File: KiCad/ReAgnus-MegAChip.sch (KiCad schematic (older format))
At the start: 40 parts, among them J3 Conn_01x03, J4 Conn_01x01, J5 Conn_01x01, J6 Conn_01x01, J7 Conn_01x01, U1 PLCC-84-Plug, U2 LM1117-3.3, U3 SN74CBTD16210, U4 SN74CBTD16210, U5 SN74CBTD16210, U6 SN74CBTD16210, U8 74LVC1G07, U9 Agnus_TH_plug_pins

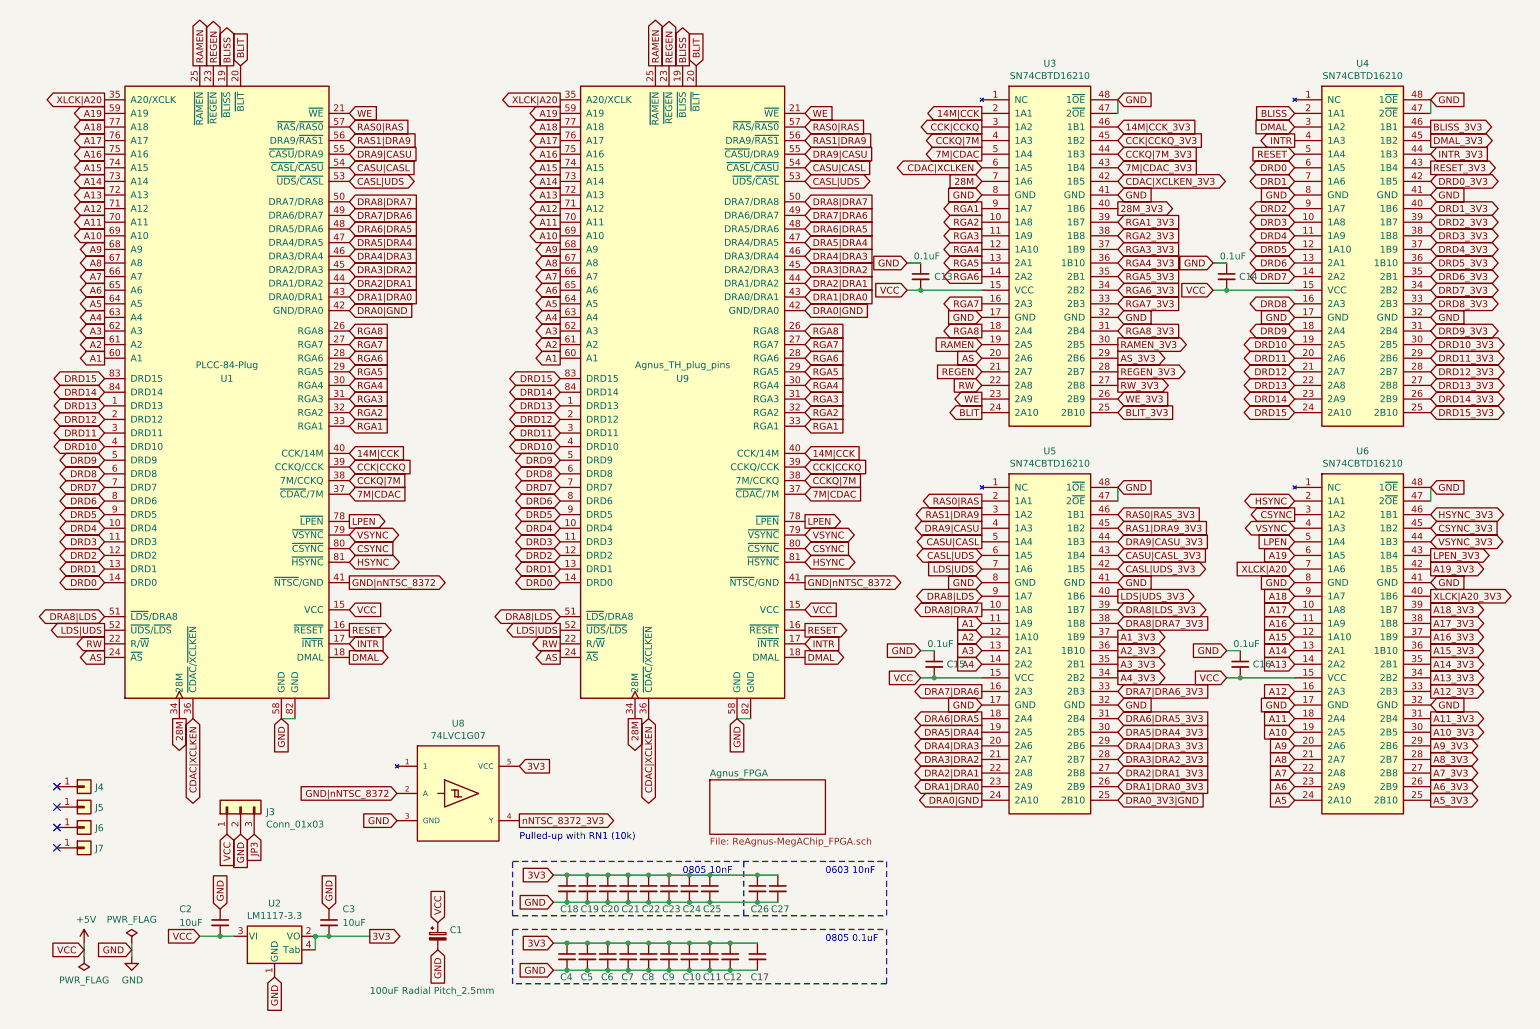
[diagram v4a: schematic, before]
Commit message: fixed typo XLCK to XCLK on (XCLK/A20) net
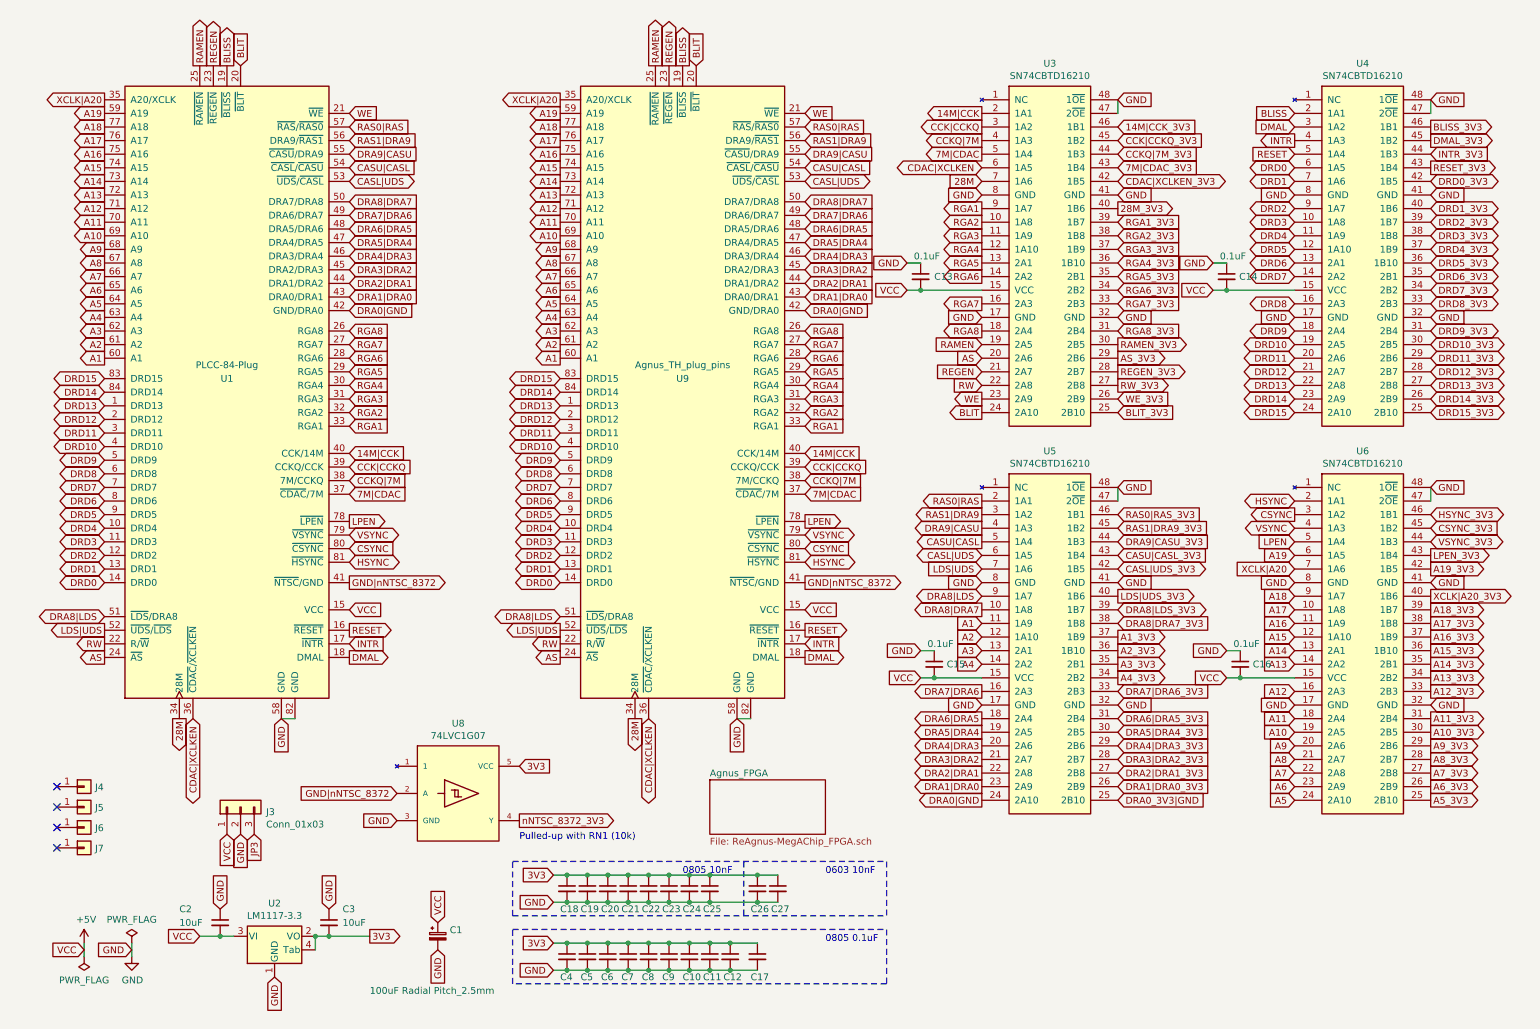
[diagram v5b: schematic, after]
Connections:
- net XLCK|A20 renamed XCLK|A20
- net XLCK|A20_3V3 renamed XCLK|A20_3V3
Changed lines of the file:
@@
 DRD0
 Text GLabel 1000 1150 0    50   Output ~ 0
-XLCK|A20
+XCLK|A20
 Text GLabel 1000 3050 0    50   Output ~ 0
 A1
@@
 DRD15
 Text GLabel 9750 4600 0    50   Input ~ 0
-XLCK|A20
+XCLK|A20
 Text GLabel 7450 4800 0    50   BiDi ~ 0
 DRA8|LDS
@@
 DRD0
 Text GLabel 4350 1150 0    50   Output ~ 0
-XLCK|A20
+XCLK|A20
 Text GLabel 4350 3050 0    50   Output ~ 0
 A1
@@
 GND
 Text GLabel 10750 4800 2    50   Output ~ 0
-XLCK|A20_3V3
+XCLK|A20_3V3
 Text GLabel 10750 4000 2    50   Input ~ 0
 GND

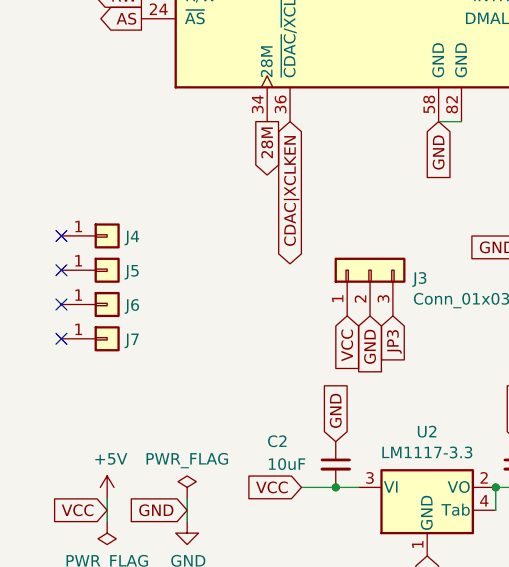
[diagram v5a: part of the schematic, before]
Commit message: Changed to 6 mil routing and to updated PLCC-footprint with 0.6mm pinholes and fixed dimensions for homebrew PLCC-84-plug
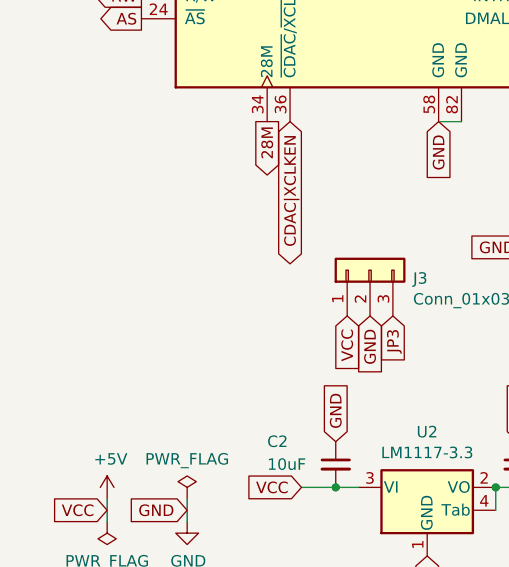
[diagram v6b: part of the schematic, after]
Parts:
- removed J4, J5, J6, J7: Conn_01x01, Connector_PinHeader_2.54mm:PinHeader_1x01_P2.54mm_Vertical, symbol Connector_Generic:Conn_01x01
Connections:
- no-connect marks 4 -> 0
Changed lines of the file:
@@
 Text GLabel 1000 5250 0    50   Output ~ 0
 AS
-$Comp
-L Connector_Generic:Conn_01x01 J4
-U 1 1 60D1FBEB
-P 850 6200
-F 0 "J4" H 930 6196 50  0000 L CNN
-F 1 "Conn_01x01" H 930 6151 50  0001 L CNN
-F 2 "Connector_PinHeader_2.54mm:PinHeader_1x01_P2.54mm_Vertical" H 850 6200 50  0001 C CNN
-F 3 "~" H 850 6200 50  0001 C CNN
-	1    850  6200
-	1    0    0    -1
-$EndComp
-$Comp
-L Connector_Generic:Conn_01x01 J5
-U 1 1 60D20CDD
-P 850 6350
-F 0 "J5" H 930 6346 50  0000 L CNN
-F 1 "Conn_01x01" H 930 6301 50  0001 L CNN
-F 2 "Connector_PinHeader_2.54mm:PinHeader_1x01_P2.54mm_Vertical" H 850 6350 50  0001 C CNN
-F 3 "~" H 850 6350 50  0001 C CNN
-	1    850  6350
-	1    0    0    -1
-$EndComp
-$Comp
-L Connector_Generic:Conn_01x01 J6
-U 1 1 60D21648
-P 850 6500
-F 0 "J6" H 930 6496 50  0000 L CNN
-F 1 "Conn_01x01" H 930 6451 50  0001 L CNN
-F 2 "Connector_PinHeader_2.54mm:PinHeader_1x01_P2.54mm_Vertical" H 850 6500 50  0001 C CNN
-F 3 "~" H 850 6500 50  0001 C CNN
-	1    850  6500
-	1    0    0    -1
-$EndComp
-$Comp
-L Connector_Generic:Conn_01x01 J7
-U 1 1 60D21D5E
-P 850 6650
-F 0 "J7" H 930 6646 50  0000 L CNN
-F 1 "Conn_01x01" H 930 6601 50  0001 L CNN
-F 2 "Connector_PinHeader_2.54mm:PinHeader_1x01_P2.54mm_Vertical" H 850 6650 50  0001 C CNN
-F 3 "~" H 850 6650 50  0001 C CNN
-	1    850  6650
-	1    0    0    -1
-$EndComp
-NoConn ~ 650  6200
-NoConn ~ 650  6350
-NoConn ~ 650  6500
-NoConn ~ 650  6650
 Text GLabel 2000 6550 3    50   Input ~ 0
 GND

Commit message: Changed level shifters from SN74CBTD16210DGGR (TSSOP-48) to SN74CBT16210CDGVR (TVSOP-48) and added a 4.3V LDO regulator TPS73643DBV and re-routed.
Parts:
- added C28: 10uF, Capacitor_SMD:C_1206_3216Metric_Pad1.33x1.80mm_HandSolder, symbol Device:C_Small
- added C29: 0.1uF, Capacitor_SMD:C_0603_1608Metric_Pad1.08x0.95mm_HandSolder, symbol Device:C_Small
- added C30: 10uF, Capacitor_SMD:C_0805_2012Metric_Pad1.18x1.45mm_HandSolder, symbol Device:C_Small
- added U13: TPS73643DBV, Package_TO_SOT_SMD:SOT-23-5, symbol Regulator_Linear:TPS73643DBV
- U3, U4, U5, U6: value SN74CBTD16210 -> SN74CBT16210; footprint Package_SO:TSSOP-48_6.1x12.5mm_P0.5mm -> Package_SO:TSSOP-48_4.4x9.7mm_P0.4mm; symbol ReAgnus-MegAChip:SN74CBTD16210 -> ReAgnus-MegAChip:SN74CBT16210
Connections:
- net +5V: now also C28.1, U13.1 (IN), U13.3 (EN); no longer C13.2, C14.2, C15.2, C16.2, U3.15 (VCC), U4.15 (VCC), U5.15 (VCC), U6.15 (VCC)
- net GND: now also C28.2, C29.2, C30.2, U13.2 (GND)
- new net: C29.1, U13.4 (NR)
- new net 4V3: C13.2, C14.2, C15.2, C16.2, C30.1, U13.5 (OUT), U3.15 (VCC), U4.15 (VCC), U5.15 (VCC), U6.15 (VCC)
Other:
- moved on the sheet: J3
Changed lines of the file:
@@
 Text GLabel 1550 5700 3    50   Output ~ 0
 28M
-Text GLabel 1650 5700 3    50   BiDi ~ 0
-CDAC|XCLKEN
 Wire Wire Line
 	2300 5700 2400 5700
@@
 Text GLabel 1000 5250 0    50   Output ~ 0
 AS
-Text GLabel 2000 6550 3    50   Input ~ 0
+Text GLabel 2350 6700 3    50   Input ~ 0
 GND
 Wire Wire Line
@@
 $EndComp
 $Comp
-L ReAgnus-MegAChip:SN74CBTD16210 U6
+L ReAgnus-MegAChip:SN74CBT16210 U6
 U 1 1 632E773E
 P 10250 5100
 F 0 "U6" H 10250 6467 50  0000 C CNN
-F 1 "SN74CBTD16210" H 10250 6376 50  0000 C CNN
-F 2 "Package_SO:TSSOP-48_6.1x12.5mm_P0.5mm" H 11900 5550 50  0001 C CNN
+F 1 "SN74CBT16210" H 10250 6376 50  0000 C CNN
+F 2 "Package_SO:TSSOP-48_4.4x9.7mm_P0.4mm" H 11900 5550 50  0001 C CNN
 F 3 "" H 11900 5550 50  0001 C CNN
 	1    10250 5100
@@
 A1_3V3
 $Comp
-L ReAgnus-MegAChip:SN74CBTD16210 U4
+L ReAgnus-MegAChip:SN74CBT16210 U4
 U 1 1 633D158E
 P 10250 2250
 F 0 "U4" H 10250 3617 50  0000 C CNN
-F 1 "SN74CBTD16210" H 10250 3526 50  0000 C CNN
-F 2 "Package_SO:TSSOP-48_6.1x12.5mm_P0.5mm" H 11900 2700 50  0001 C CNN
+F 1 "SN74CBT16210" H 10250 3526 50  0000 C CNN
+F 2 "Package_SO:TSSOP-48_4.4x9.7mm_P0.4mm" H 11900 2700 50  0001 C CNN
 F 3 "" H 11900 2700 50  0001 C CNN
 	1    10250 2250
@@
 LPEN_3V3
 $Comp
-L ReAgnus-MegAChip:SN74CBTD16210 U3
+L ReAgnus-MegAChip:SN74CBT16210 U3
 U 1 1 634B56C3
 P 7950 2250
 F 0 "U3" H 7950 3617 50  0000 C CNN
-F 1 "SN74CBTD16210" H 7950 3526 50  0000 C CNN
-F 2 "Package_SO:TSSOP-48_6.1x12.5mm_P0.5mm" H 9600 2700 50  0001 C CNN
+F 1 "SN74CBT16210" H 7950 3526 50  0000 C CNN
+F 2 "Package_SO:TSSOP-48_4.4x9.7mm_P0.4mm" H 9600 2700 50  0001 C CNN
 F 3 "" H 9600 2700 50  0001 C CNN
 	1    7950 2250
@@
 GND
 $Comp
-L ReAgnus-MegAChip:SN74CBTD16210 U5
+L ReAgnus-MegAChip:SN74CBT16210 U5
 U 1 1 634CD3ED
 P 7950 5100
 F 0 "U5" H 7950 6467 50  0000 C CNN
-F 1 "SN74CBTD16210" H 7950 6376 50  0000 C CNN
-F 2 "Package_SO:TSSOP-48_6.1x12.5mm_P0.5mm" H 9600 5550 50  0001 C CNN
+F 1 "SN74CBT16210" H 7950 6376 50  0000 C CNN
+F 2 "Package_SO:TSSOP-48_4.4x9.7mm_P0.4mm" H 9600 5550 50  0001 C CNN
 F 3 "" H 9600 5550 50  0001 C CNN
 	1    7950 5100
@@
 GND
 Text GLabel 9150 2550 0    50   Input ~ 0
-VCC
+4V3
 Text GLabel 10750 1650 2    50   Output ~ 0
 RESET_3V3
@@
 	9150 2350 9250 2350
 Text GLabel 7000 5400 0    50   Input ~ 0
-VCC
+4V3
 Text GLabel 7000 5200 0    50   Input ~ 0
 GND
@@
 	7000 5200 7100 5200
 Text GLabel 9250 5400 0    50   Input ~ 0
-VCC
+4V3
 Text GLabel 9250 5200 0    50   Input ~ 0
 GND
@@
 Connection ~ 7100 5400
 Text GLabel 6900 2550 0    50   Input ~ 0
-VCC
+4V3
 Text GLabel 6900 2350 0    50   Input ~ 0
 GND
@@
 Text GLabel 1700 7300 0    50   Input ~ 0
 VCC
-Text GLabel 1900 6550 3    50   Input ~ 0
+Text GLabel 2250 6700 3    50   Input ~ 0
 VCC
 Text GLabel 1850 7100 1    50   Input ~ 0
@@
 Wire Wire Line
 	5450 7050 5800 7050
-Text GLabel 2100 6550 3    50   Input ~ 0
+Text GLabel 2450 6700 3    50   Input ~ 0
 JP3
 $Comp
 L Connector_Generic:Conn_01x03 J3
 U 1 1 63977F90
-P 2000 6350
-F 0 "J3" V 1964 6162 50  0000 R CNN
-F 1 "Conn_01x03" V 1873 6162 50  0000 R CNN
-F 2 "Connector_PinHeader_2.54mm:PinHeader_1x03_P2.54mm_Vertical" H 2000 6350 50  0001 C CNN
-F 3 "~" H 2000 6350 50  0001 C CNN
-	1    2000 6350
+P 2350 6500
+F 0 "J3" V 2314 6312 50  0000 R CNN
+F 1 "Conn_01x03" V 2223 6312 50  0000 R CNN
+F 2 "Connector_PinHeader_2.54mm:PinHeader_1x03_P2.54mm_Vertical" H 2350 6500 50  0001 C CNN
+F 3 "~" H 2350 6500 50  0001 C CNN
+	1    2350 6500
 	0    -1   -1   0
 $EndComp
+$Comp
+L Regulator_Linear:TPS73643DBV U13
+U 1 1 661AF7F8
+P 1150 6650
+F 0 "U13" H 1150 7017 50  0000 C CNN
+F 1 "TPS73643DBV" H 1150 6926 50  0000 C CNN
+F 2 "Package_TO_SOT_SMD:SOT-23-5" H 1150 6975 50  0001 C CIN
+F 3 "http://www.ti.com/lit/ds/symlink/tps736.pdf" H 1150 6600 50  0001 C CNN
+	1    1150 6650
+	1    0    0    -1
+$EndComp
+Text GLabel 1650 5700 3    50   BiDi ~ 0
+CDAC|XCLKEN
+$Comp
+L Device:C_Small C28
+U 1 1 661B6113
+P 600 6650
+AR Path="/661B6113" Ref="C28"  Part="1"
+AR Path="/632D3BDF/661B6113" Ref="C?"  Part="1"
+AR Path="/632F104D/661B6113" Ref="C?"  Part="1"
+F 0 "C28" H 550 6950 50  0000 L CNN
+F 1 "10uF" H 500 6850 50  0000 L CNN
+F 2 "Capacitor_SMD:C_1206_3216Metric_Pad1.33x1.80mm_HandSolder" H 600 6650 50  0001 C CNN
+F 3 "~" H 600 6650 50  0001 C CNN
+	1    600  6650
+	1    0    0    -1
+$EndComp
+Wire Wire Line
+	600  6750 600  6950
+Wire Wire Line
+	600  6950 1150 6950
+Wire Wire Line
+	600  6550 750  6550
+Wire Wire Line
+	750  6550 750  6650
+Connection ~ 750  6550
+$Comp
+L Device:C_Small C30
+U 1 1 661BF4C9
+P 1700 6650
+AR Path="/661BF4C9" Ref="C30"  Part="1"
+AR Path="/632D3BDF/661BF4C9" Ref="C?"  Part="1"
+AR Path="/632F104D/661BF4C9" Ref="C?"  Part="1"
+F 0 "C30" H 1650 6950 50  0000 L CNN
+F 1 "10uF" H 1600 6850 50  0000 L CNN
+F 2 "Capacitor_SMD:C_0805_2012Metric_Pad1.18x1.45mm_HandSolder" H 1700 6650 50  0001 C CNN
+F 3 "~" H 1700 6650 50  0001 C CNN
+	1    1700 6650
+	1    0    0    -1
+$EndComp
+Wire Wire Line
+	1550 6550 1700 6550
+Connection ~ 1700 6550
+Wire Wire Line
+	1700 6550 1800 6550
+Text GLabel 1800 6550 2    50   Output ~ 0
+4V3
+Wire Wire Line
+	1150 6950 1550 6950
+Wire Wire Line
+	1700 6950 1700 6750
+Connection ~ 1150 6950
+$Comp
+L Device:C_Small C29
+U 1 1 661C65A2
+P 1550 6750
+F 0 "C29" H 1550 6600 50  0000 L CNN
+F 1 "0.1uF" H 1300 6600 50  0000 L CNN
+F 2 "Capacitor_SMD:C_0603_1608Metric_Pad1.08x0.95mm_HandSolder" H 1550 6750 50  0001 C CNN
+F 3 "~" H 1550 6750 50  0001 C CNN
+	1    1550 6750
+	1    0    0    -1
+$EndComp
+Wire Wire Line
+	1550 6850 1550 6950
+Connection ~ 1550 6950
+Wire Wire Line
+	1550 6950 1700 6950
+Text GLabel 600  6550 0    50   Input ~ 0
+VCC
+Text GLabel 600  6950 3    50   Input ~ 0
+GND
 $EndSCHEMATC

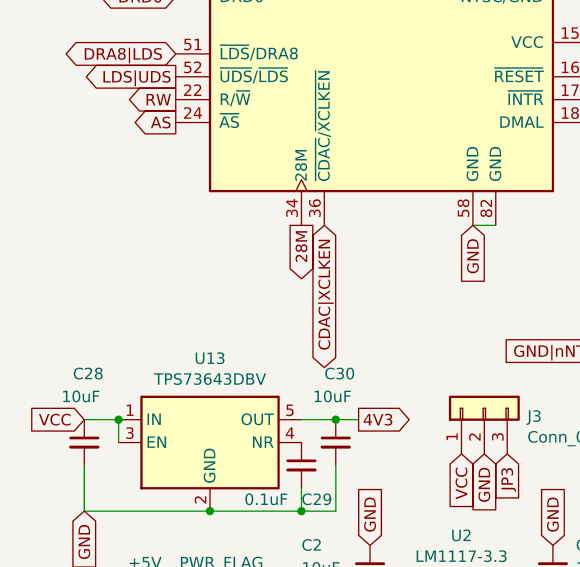
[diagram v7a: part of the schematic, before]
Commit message: Changed to a four layer stackup, GND and a 3V3 as inner layers, added a MountingHole_2.2mm_M2 for proper grounding via a ring lug connector on a thick jumper wire
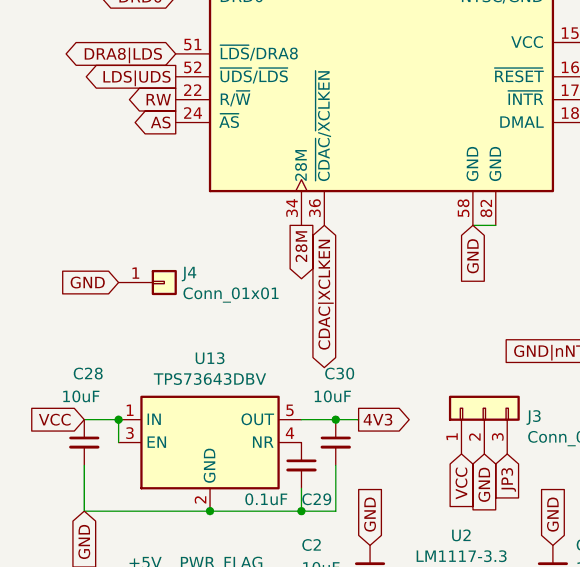
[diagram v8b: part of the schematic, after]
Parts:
- added J4: Conn_01x01, MountingHole:MountingHole_2.2mm_M2_Pad_Via, symbol Connector_Generic:Conn_01x01
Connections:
- net GND: now also J4.1 (Pin_1)
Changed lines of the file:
@@
 Text GLabel 600  6950 3    50   Input ~ 0
 GND
+$Comp
+L Connector_Generic:Conn_01x01 J4
+U 1 1 669038FF
+P 950 5950
+F 0 "J4" H 1030 5992 50  0000 L CNN
+F 1 "Conn_01x01" H 1030 5901 50  0000 L CNN
+F 2 "MountingHole:MountingHole_2.2mm_M2_Pad_Via" H 950 5950 50  0001 C CNN
+F 3 "~" H 950 5950 50  0001 C CNN
+	1    950  5950
+	1    0    0    -1
+$EndComp
+Text GLabel 750  5950 0    50   Input ~ 0
+GND
 $EndSCHEMATC
